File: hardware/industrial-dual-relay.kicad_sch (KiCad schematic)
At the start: 27 parts

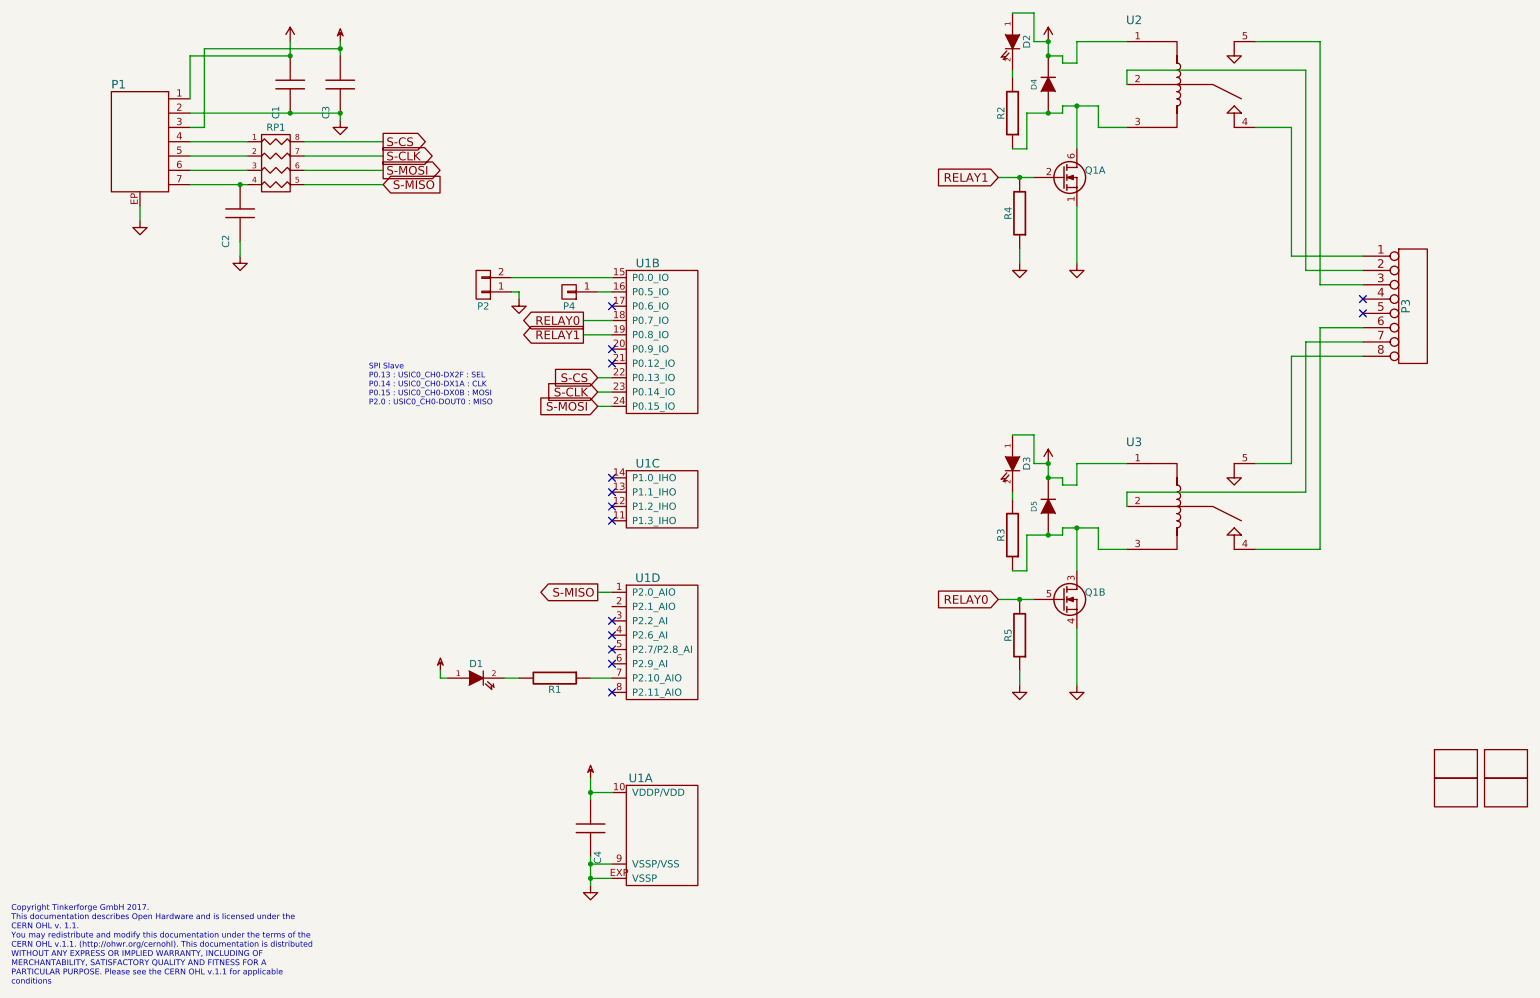
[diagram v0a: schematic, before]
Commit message: changed footprint from 8p-oq to 8p-oq-230v
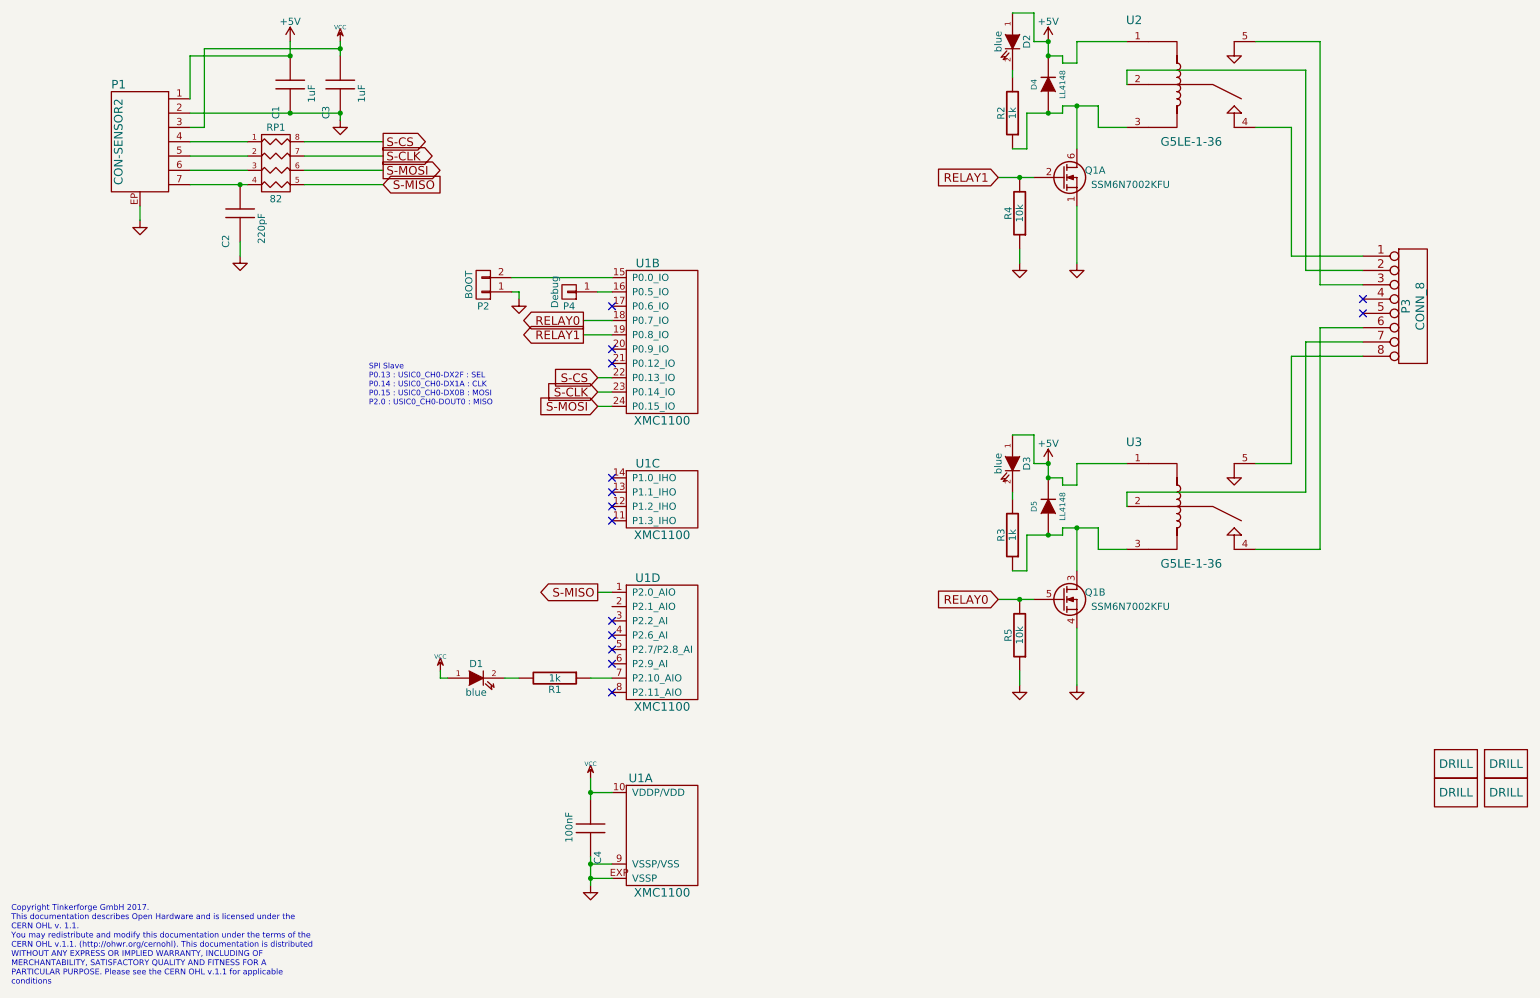
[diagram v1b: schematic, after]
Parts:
- C1, C3: value (none) -> 1uF; footprint (none) -> kicad-libraries:C0603F
- C2: value (none) -> 220pF; footprint (none) -> kicad-libraries:C0402F
- C4: value (none) -> 100nF; footprint (none) -> kicad-libraries:C0603F
- D1, D2, D3: value (none) -> blue; footprint (none) -> kicad-libraries:D0603E
- D4, D5: value (none) -> LL4148; footprint (none) -> kicad-libraries:SOD-123
- P1: value (none) -> CON-SENSOR2; footprint (none) -> kicad-libraries:CON-SENSOR2
- P2: value (none) -> BOOT; footprint (none) -> kicad-libraries:SolderJumper
- P3: value (none) -> CONN_8; footprint (none) -> kicad-libraries:OQ_8P_230V
- P4: value (none) -> Debug; footprint (none) -> kicad-libraries:DEBUG_PAD
- Q1: value (none) -> SSM6N7002KFU; footprint (none) -> kicad-libraries:SOT363
- R1, R2, R3: value (none) -> 1k; footprint (none) -> kicad-libraries:R0603F
- R4, R5: value (none) -> 10k; footprint (none) -> kicad-libraries:R0402F
- RP1: value (none) -> 82; footprint (none) -> kicad-libraries:4X0402
- U1: value (none) -> XMC1100; footprint (none) -> kicad-libraries:QFN24-4x4mm-0.5mm
- U2, U3: value (none) -> G5LE-1-36; footprint (none) -> kicad-libraries:G5LE-1
- U4, U5, U6, U7: value (none) -> DRILL; footprint (none) -> kicad-libraries:DRILL_NP

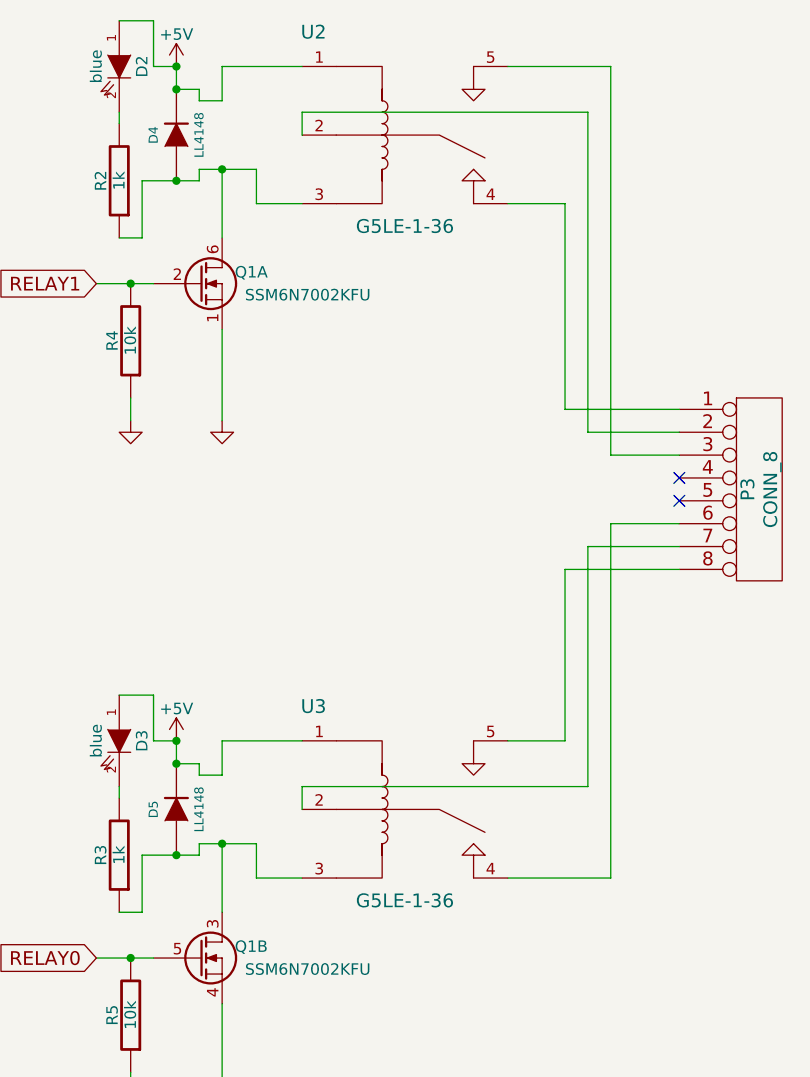
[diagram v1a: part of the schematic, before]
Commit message: Version 1.1: changed relay, more clearance
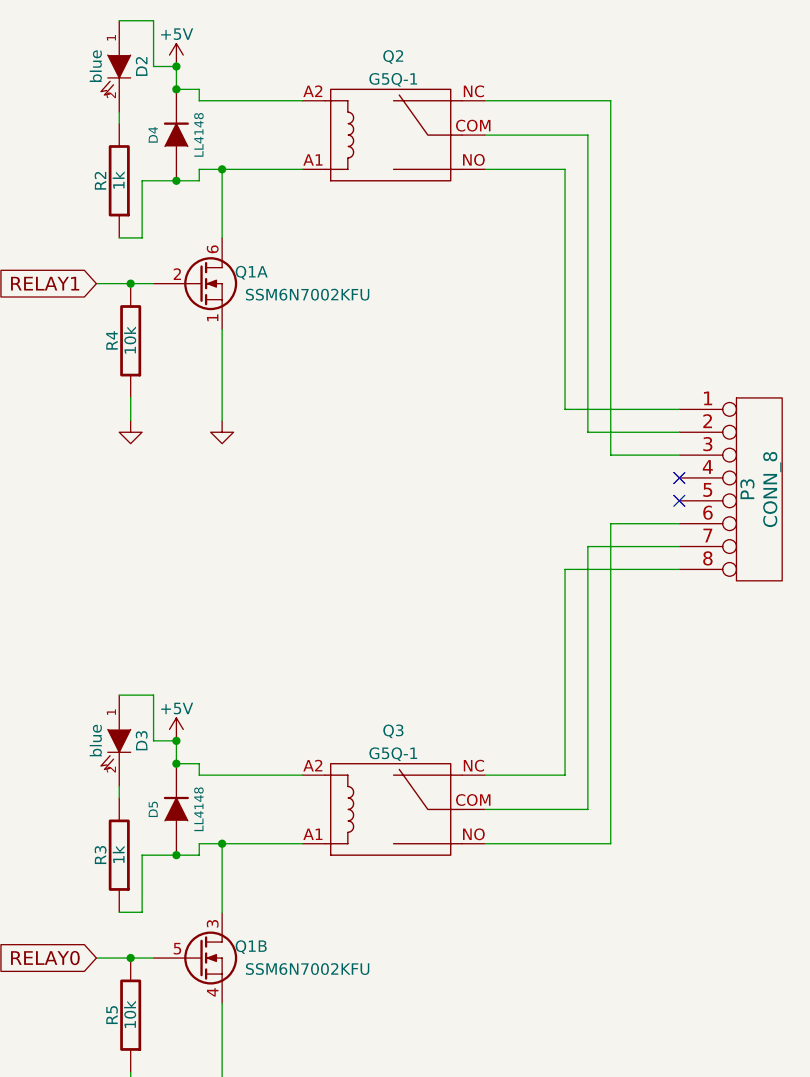
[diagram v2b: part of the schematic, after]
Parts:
- removed U2, U3: G5LE-1-36, kicad-libraries:G5LE-1, symbol tinkerforge:ORWH-SX
- added Q2, Q3: G5Q-1, kicad-libraries:G5Q-1, symbol tinkerforge:G5Q-1
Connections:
- net +5V: now also Q2.A2, Q3.A2
- net at D5.1 (A), Q1.3 (D2), R3.1: now also Q3.A1
- net at D4.1 (A), Q1.6 (D1), R2.1: now also Q2.A1
- net at P3.2: now also Q2.COM
- net at P3.1: now also Q2.NO
- net at P3.3: now also Q2.NC
- net at P3.7: now also Q3.COM
- net at P3.6: now also Q3.NO
- net at P3.8: now also Q3.NC

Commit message: updated diode to minimelf footprint
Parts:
- D4, D5: footprint kicad-libraries:SOD-123 -> kicad-libraries:MiniMelf
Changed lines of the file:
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@@
       (effects (font (size 1.016 1.016)))
     )
-    (property "Footprint" "kicad-libraries:SOD-123" (id 2) (at 198.12 110.49 0)
+    (property "Footprint" "kicad-libraries:MiniMelf" (id 2) (at 198.12 110.49 0)
       (effects (font (size 1.524 1.524)) hide)
     )
@@
       (effects (font (size 1.016 1.016)))
     )
-    (property "Footprint" "kicad-libraries:SOD-123" (id 2) (at 198.12 35.56 0)
+    (property "Footprint" "kicad-libraries:MiniMelf" (id 2) (at 198.12 35.56 0)
       (effects (font (size 1.524 1.524)) hide)
     )
@@
     )
     (path "/00000000-0000-0000-0000-0000590b4fd5"
-      (reference "D4") (unit 1) (value "LL4148") (footprint "kicad-libraries:SOD-123")
+      (reference "D4") (unit 1) (value "LL4148") (footprint "kicad-libraries:MiniMelf")
     )
     (path "/00000000-0000-0000-0000-000059008c09"
-      (reference "D5") (unit 1) (value "LL4148") (footprint "kicad-libraries:SOD-123")
+      (reference "D5") (unit 1) (value "LL4148") (footprint "kicad-libraries:MiniMelf")
     )
     (path "/00000000-0000-0000-0000-00004c5fcf27"

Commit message: Version 1.2: Updated relay footprint
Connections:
- net GND: now also U1.20 (P0.9_IO)
- no-connect marks 14 -> 13
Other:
- note added: "Version Detection V1.2"
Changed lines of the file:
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@@
   (no_connect (at 120.65 110.49))
   (no_connect (at 120.65 138.43))
-  (no_connect (at 120.65 82.55))
   (no_connect (at 120.65 74.93))
   (no_connect (at 254 76.2))
@@
     (stroke (width 0) (type default) (color 0 0 0 0))
   )
+  (wire (pts (xy 120.65 82.55) (xy 90.17 82.55))
+    (stroke (width 0) (type default) (color 0 0 0 0))
+  )
   (wire (pts (xy 116.84 173.99) (xy 116.84 176.53))
     (stroke (width 0) (type default) (color 0 0 0 0))
@@
   )
   (wire (pts (xy 243.84 110.49) (xy 232.41 110.49))
+    (stroke (width 0) (type default) (color 0 0 0 0))
+  )
+  (wire (pts (xy 90.17 82.55) (xy 90.17 83.82))
     (stroke (width 0) (type default) (color 0 0 0 0))
   )
@@
   )
   (text "SPI Slave\nP0.13 : USIC0_CH0-DX2F : SEL\nP0.14 : USIC0_CH0-DX1A : CLK\nP0.15 : USIC0_CH0-DX0B : MOSI\nP2.0 : USIC0_CH0-DOUT0 : MISO"
-    (at 77.47 92.71 0)
+    (at 138.43 85.09 0)
     (effects (font (size 0.9906 0.9906)) (justify left bottom))
+  )
+  (text "Version Detection V1.2" (at 66.04 83.82 0)
+    (effects (font (size 1.27 1.27)) (justify left bottom))
   )
   (global_label "S-CLK" (shape input) (at 118.11 90.17 180) (fields_autoplaced)
@@
     (pin "1")
   )
+  (symbol (lib_id "tinkerforge:GND") (at 90.17 83.82 0) (unit 1)
+    (in_bom yes) (on_board yes)
+    (property "Reference" "#PWR0101" (id 0) (at 90.17 83.82 0)
+      (effects (font (size 0.762 0.762)) hide)
+    )
+    (property "Value" "GND" (id 1) (at 90.17 85.598 0)
+      (effects (font (size 0.762 0.762)) hide)
+    )
+    (property "Footprint" "" (id 2) (at 90.17 83.82 0)
+      (effects (font (size 1.524 1.524)) hide)
+    )
+    (property "Datasheet" "" (id 3) (at 90.17 83.82 0)
+      (effects (font (size 1.524 1.524)) hide)
+    )
+    (pin "1")
+  )
   (symbol (lib_id "tinkerforge:G5Q-1") (at 222.25 110.49 0) (mirror x) (unit 1)
     (in_bom yes) (on_board yes) (fields_autoplaced)
@@
       (reference "#PWR015") (unit 1) (value "GND") (footprint "")
     )
+    (path "/1af1904e-1605-4556-8447-dce9c4fabbf9"
+      (reference "#PWR0101") (unit 1) (value "GND") (footprint "")
+    )
     (path "/00000000-0000-0000-0000-00005a26ef62"

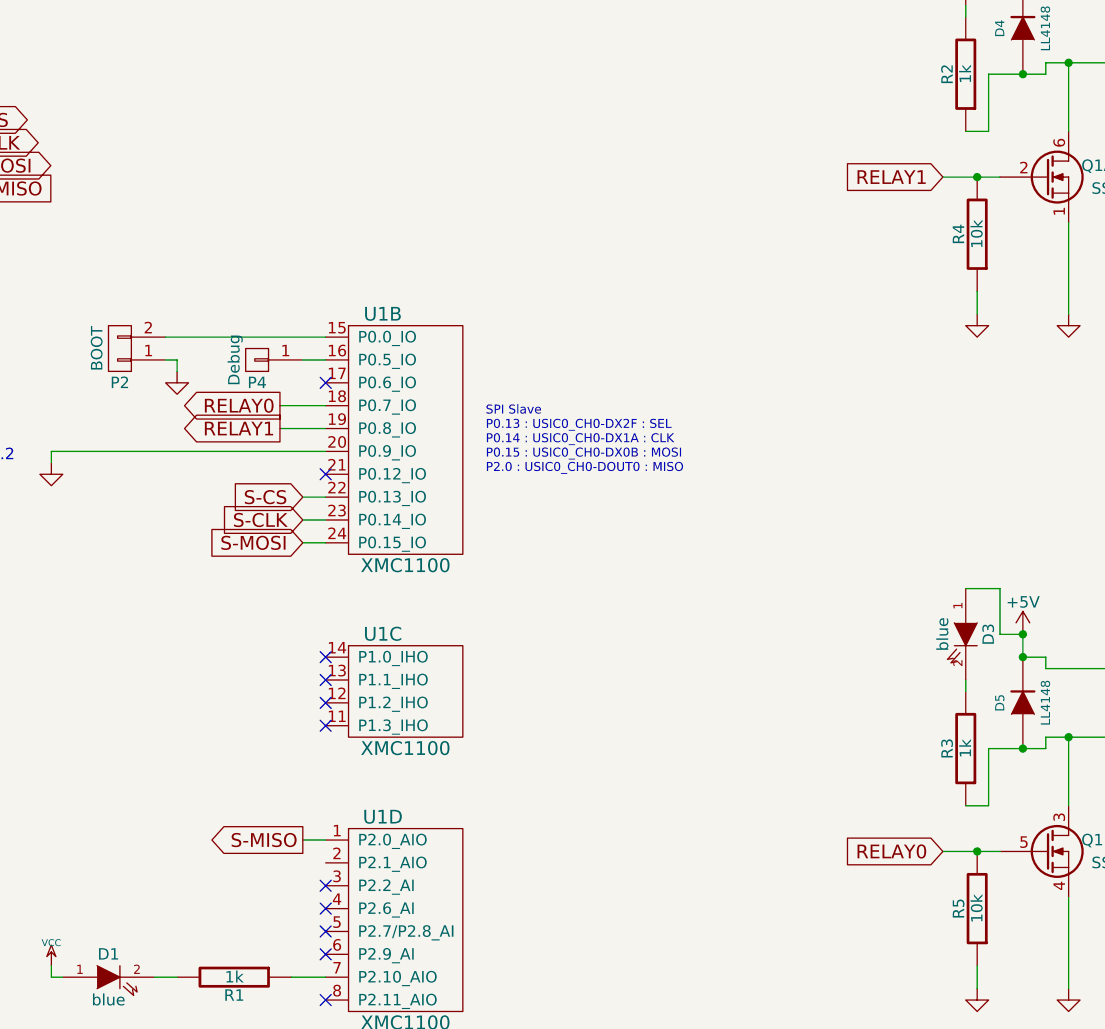
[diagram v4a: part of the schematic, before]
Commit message: changed relay0 and relay1 label
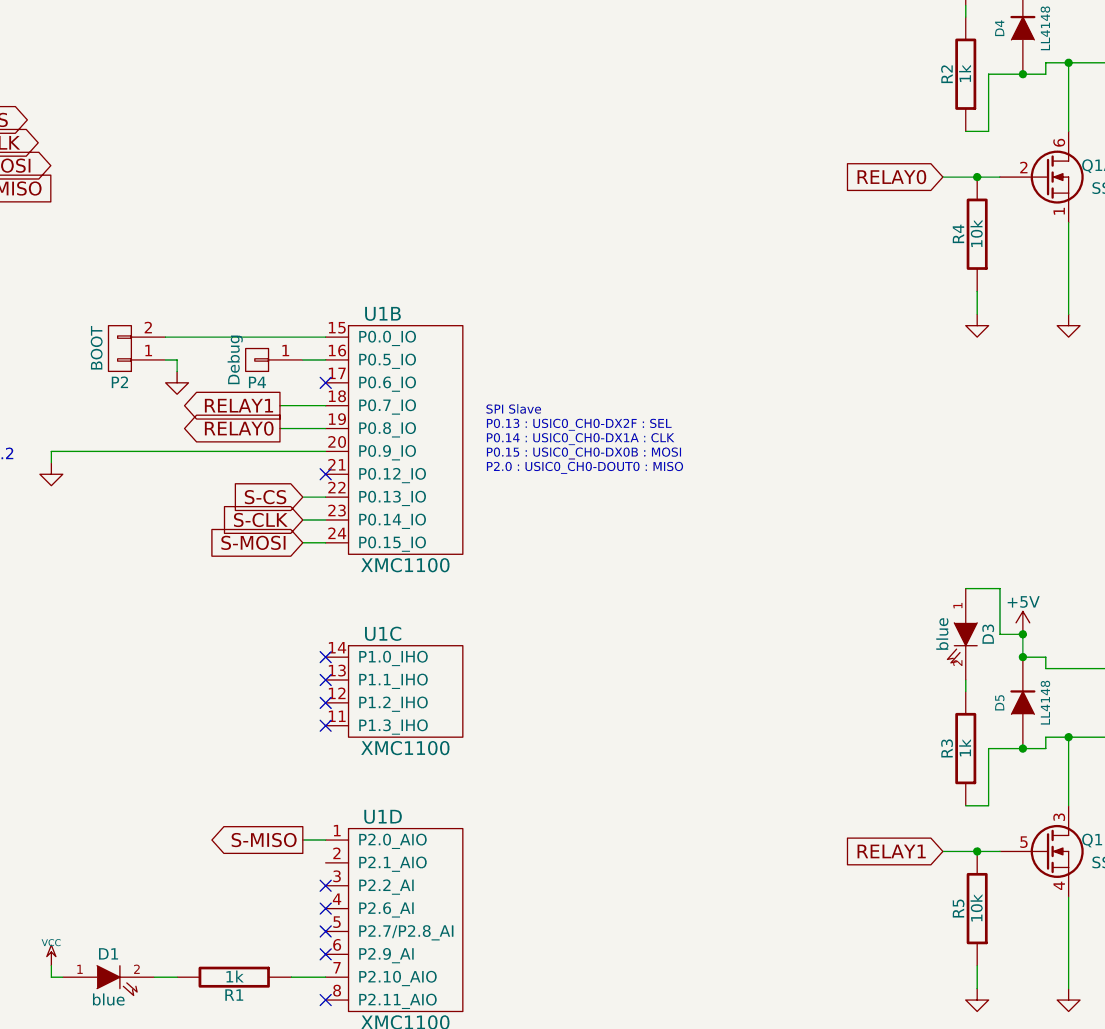
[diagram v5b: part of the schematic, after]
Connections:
- net RELAY0: now also Q1.2 (G1), R4.2, U1.19 (P0.8_IO); no longer Q1.5 (G2), R5.2, U1.18 (P0.7_IO)
- net RELAY1: now also Q1.5 (G2), R5.2, U1.18 (P0.7_IO); no longer Q1.2 (G1), R4.2, U1.19 (P0.8_IO)
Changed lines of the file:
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@@
     )
   )
-  (global_label "RELAY0" (shape input) (at 189.23 127 180) (fields_autoplaced)
+  (global_label "RELAY1" (shape input) (at 189.23 127 180) (fields_autoplaced)
     (effects (font (size 1.524 1.524)) (justify right))
-    (property "Intersheet References" "${INTERSHEET_REFS}" (id 0) (at 0 0 0)
-      (effects (font (size 1.27 1.27)) hide)
+    (property "Intersheet References" "${INTERSHEET_REFS}" (id 0) (at 178.2405 126.9048 0)
+      (effects (font (size 1.524 1.524)) (justify right) hide)
     )
   )
@@
     )
   )
-  (global_label "RELAY1" (shape output) (at 115.57 80.01 180) (fields_autoplaced)
+  (global_label "RELAY0" (shape output) (at 115.57 80.01 180) (fields_autoplaced)
     (effects (font (size 1.524 1.524)) (justify right))
-    (property "Intersheet References" "${INTERSHEET_REFS}" (id 0) (at 0 0 0)
-      (effects (font (size 1.27 1.27)) hide)
+    (property "Intersheet References" "${INTERSHEET_REFS}" (id 0) (at 104.5805 79.9148 0)
+      (effects (font (size 1.524 1.524)) (justify right) hide)
     )
   )
@@
     )
   )
-  (global_label "RELAY0" (shape output) (at 115.57 77.47 180) (fields_autoplaced)
+  (global_label "RELAY1" (shape output) (at 115.57 77.47 180) (fields_autoplaced)
     (effects (font (size 1.524 1.524)) (justify right))
-    (property "Intersheet References" "${INTERSHEET_REFS}" (id 0) (at 0 0 0)
-      (effects (font (size 1.27 1.27)) hide)
+    (property "Intersheet References" "${INTERSHEET_REFS}" (id 0) (at 104.5805 77.3748 0)
+      (effects (font (size 1.524 1.524)) (justify right) hide)
     )
   )
-  (global_label "RELAY1" (shape input) (at 189.23 52.07 180) (fields_autoplaced)
+  (global_label "RELAY0" (shape input) (at 189.23 52.07 180) (fields_autoplaced)
     (effects (font (size 1.524 1.524)) (justify right))
-    (property "Intersheet References" "${INTERSHEET_REFS}" (id 0) (at 0 0 0)
-      (effects (font (size 1.27 1.27)) hide)
+    (property "Intersheet References" "${INTERSHEET_REFS}" (id 0) (at 178.2405 51.9748 0)
+      (effects (font (size 1.524 1.524)) (justify right) hide)
     )
   )
